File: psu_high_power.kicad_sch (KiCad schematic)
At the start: 4 parts, among them U3 CH224K

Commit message: Final schematic before review.
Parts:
- renumbered C1 to C3, R2 to R3, R1 to R4, U3 to U4
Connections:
- no-connect marks 1 -> 2
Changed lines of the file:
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@@
 	)
 	(no_connect
-		(at 154.94 63.5)
+		(at 92.71 62.23)
+	)
+	(no_connect
+		(at 92.71 59.69)
+	)
+	(wire
+		(pts
+			(xy 99.06 57.15) (xy 99.06 34.29)
+		)
+		(stroke
+			(width 0)
+			(type default)
+		)
+	)
+	(wire
+		(pts
+			(xy 43.18 59.69) (xy 72.39 59.69)
+		)
+		(stroke
+			(width 0)
+			(type default)
+		)
 	)
 	(wire
@@
 	(wire
 		(pts
-			(xy 99.06 57.15) (xy 99.06 34.29)
-		)
-		(stroke
-			(width 0)
-			(type default)
-		)
-	)
-	(wire
-		(pts
-			(xy 43.18 59.69) (xy 72.39 59.69)
-		)
-		(stroke
-			(width 0)
-			(type default)
-		)
-	)
-	(wire
-		(pts
 			(xy 92.71 57.15) (xy 99.06 57.15)
 		)
@@
 	(wire
 		(pts
-			(xy 99.06 34.29) (xy 85.09 34.29)
-		)
-		(stroke
-			(width 0)
-			(type default)
-		)
-	)
-	(wire
-		(pts
 			(xy 92.71 52.07) (xy 116.84 52.07)
 		)
@@
 		(pts
 			(xy 66.04 34.29) (xy 85.09 34.29)
+		)
+		(stroke
+			(width 0)
+			(type default)
+		)
+	)
+	(wire
+		(pts
+			(xy 85.09 34.29) (xy 99.06 34.29)
 		)
 		(stroke
@@
 		(dnp no)
 		(fields_autoplaced yes)
-		(property "Reference" "U3"
+		(property "Reference" "U4"
 			(at 84.6933 67.31 0)
 			(effects
@@
 			(project ""
 				(path "/64404f27-cfd6-41d9-8edb-810ebab8cc14/d3bc8089-8207-4629-875b-88a1d886a985"
-					(reference "U3")
+					(reference "U4")
 					(unit 1)
 				)
@@
 		(on_board yes)
 		(dnp no)
-		(property "Reference" "R2"
+		(property "Reference" "R3"
 			(at 62.23 34.29 90)
 			(effects
@@
 			(project ""
 				(path "/64404f27-cfd6-41d9-8edb-810ebab8cc14/d3bc8089-8207-4629-875b-88a1d886a985"
-					(reference "R2")
+					(reference "R3")
 					(unit 1)
 				)
@@
 		(on_board yes)
 		(dnp no)
-		(property "Reference" "R1"
+		(property "Reference" "R4"
 			(at 62.484 43.434 90)
 			(effects
@@
 			(project ""
 				(path "/64404f27-cfd6-41d9-8edb-810ebab8cc14/d3bc8089-8207-4629-875b-88a1d886a985"
-					(reference "R1")
+					(reference "R4")
 					(unit 1)
 				)
@@
 		(dnp no)
 		(fields_autoplaced yes)
-		(property "Reference" "C1"
+		(property "Reference" "C3"
 			(at 111.76 69.8499 0)
 			(effects
@@
 			(project ""
 				(path "/64404f27-cfd6-41d9-8edb-810ebab8cc14/d3bc8089-8207-4629-875b-88a1d886a985"
-					(reference "C1")
+					(reference "C3")
 					(unit 1)
 				)

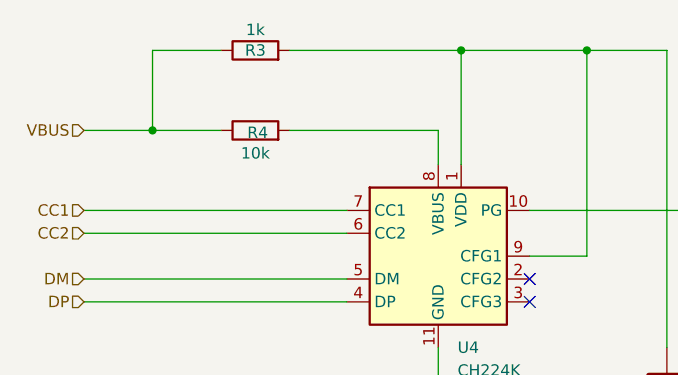
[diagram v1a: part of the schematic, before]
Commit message: Added TVS (SMAJ5.0A) to VBUS-GND Added polyfuses to both PSUs
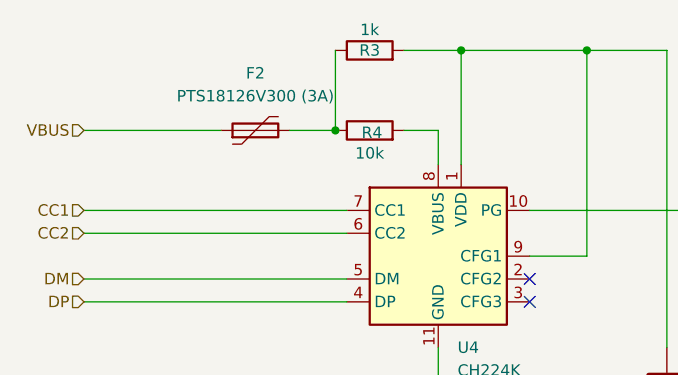
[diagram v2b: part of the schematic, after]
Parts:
- added F2: PTS18126V300 (3A), symbol Device:Polyfuse
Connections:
- net VBUS: now also F2.1; no longer R3.1, R4.1
- new net: F2.2, R3.1, R4.1
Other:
- moved on the sheet: R3, R4
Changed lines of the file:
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@@
 	(paper "A4")
+	(junction
+		(at 71.12 43.18)
+		(diameter 0)
+		(color 0 0 0 0)
+	)
 	(junction
 		(at 82.55 74.93)
@@
 	)
 	(junction
-		(at 50.8 43.18)
+		(at 99.06 34.29)
 		(diameter 0)
 		(color 0 0 0 0)
@@
 		(color 0 0 0 0)
 	)
-	(junction
-		(at 99.06 34.29)
-		(diameter 0)
-		(color 0 0 0 0)
-	)
 	(no_connect
 		(at 92.71 62.23)
@@
 	(wire
 		(pts
+			(xy 78.74 34.29) (xy 85.09 34.29)
+		)
+		(stroke
+			(width 0)
+			(type default)
+		)
+	)
+	(wire
+		(pts
 			(xy 99.06 57.15) (xy 99.06 34.29)
 		)
@@
 	(wire
 		(pts
+			(xy 66.04 43.18) (xy 71.12 43.18)
+		)
+		(stroke
+			(width 0)
+			(type default)
+		)
+	)
+	(wire
+		(pts
 			(xy 92.71 52.07) (xy 116.84 52.07)
 		)
@@
 	(wire
 		(pts
-			(xy 58.42 34.29) (xy 50.8 34.29)
-		)
-		(stroke
-			(width 0)
-			(type default)
-		)
-	)
-	(wire
-		(pts
-			(xy 66.04 43.18) (xy 82.55 43.18)
-		)
-		(stroke
-			(width 0)
-			(type default)
-		)
-	)
-	(wire
-		(pts
 			(xy 82.55 67.31) (xy 82.55 74.93)
 		)
@@
 	(wire
 		(pts
+			(xy 71.12 34.29) (xy 71.12 43.18)
+		)
+		(stroke
+			(width 0)
+			(type default)
+		)
+	)
+	(wire
+		(pts
 			(xy 82.55 80.01) (xy 86.36 80.01)
 		)
@@
 	(wire
 		(pts
-			(xy 50.8 34.29) (xy 50.8 43.18)
+			(xy 78.74 43.18) (xy 82.55 43.18)
 		)
 		(stroke
@@
 	(wire
 		(pts
-			(xy 43.18 43.18) (xy 50.8 43.18)
-		)
-		(stroke
-			(width 0)
-			(type default)
-		)
-	)
-	(wire
-		(pts
-			(xy 66.04 34.29) (xy 85.09 34.29)
+			(xy 43.18 43.18) (xy 58.42 43.18)
 		)
 		(stroke
@@
 		(pts
 			(xy 43.18 52.07) (xy 72.39 52.07)
-		)
-		(stroke
-			(width 0)
-			(type default)
-		)
-	)
-	(wire
-		(pts
-			(xy 50.8 43.18) (xy 58.42 43.18)
 		)
 		(stroke
@@
 			)
 			(justify right)
+		)
+	)
+	(symbol
+		(lib_id "Device:Polyfuse")
+		(at 62.23 43.18 90)
+		(unit 1)
+		(exclude_from_sim no)
+		(in_bom yes)
+		(on_board yes)
+		(dnp no)
+		(fields_autoplaced yes)
+		(property "Reference" "F2"
+			(at 62.23 36.83 90)
+			(effects
+				(font
+					(size 1.27 1.27)
+				)
+			)
+		)
+		(property "Value" "PTS18126V300 (3A)"
+			(at 62.23 39.37 90)
+			(effects
+				(font
+					(size 1.27 1.27)
+				)
+			)
+		)
+		(property "Footprint" ""
+			(at 67.31 41.91 0)
+			(effects
+				(font
+					(size 1.27 1.27)
+				)
+				(justify left)
+				(hide yes)
+			)
+		)
+		(property "Datasheet" "~"
+			(at 62.23 43.18 0)
+			(effects
+				(font
+					(size 1.27 1.27)
+				)
+				(hide yes)
+			)
+		)
+		(property "Description" "Resettable fuse, polymeric positive temperature coefficient"
+			(at 62.23 43.18 0)
+			(effects
+				(font
+					(size 1.27 1.27)
+				)
+				(hide yes)
+			)
+		)
+		(pin "1"
+		)
+		(pin "2"
+		)
+		(instances
+			(project ""
+				(path "/64404f27-cfd6-41d9-8edb-810ebab8cc14/d3bc8089-8207-4629-875b-88a1d886a985"
+					(reference "F2")
+					(unit 1)
+				)
+			)
 		)
 	)
@@
 	(symbol
 		(lib_id "Device:R")
-		(at 62.23 34.29 90)
+		(at 74.93 34.29 90)
 		(unit 1)
 		(exclude_from_sim no)
@@
 		(dnp no)
 		(property "Reference" "R3"
-			(at 62.23 34.29 90)
+			(at 74.93 34.29 90)
 			(effects
 				(font
@@
 		)
 		(property "Value" "1k"
-			(at 62.23 32.004 90)
+			(at 74.93 32.004 90)
 			(effects
 				(font
@@
 		)
 		(property "Footprint" ""
-			(at 62.23 36.068 90)
+			(at 74.93 36.068 90)
 			(effects
 				(font
@@
 		)
 		(property "Datasheet" "~"
-			(at 62.23 34.29 0)
+			(at 74.93 34.29 0)
 			(effects
 				(font
@@
 		)
 		(property "Description" "Resistor"
-			(at 62.23 34.29 0)
+			(at 74.93 34.29 0)
 			(effects
 				(font
@@
 	(symbol
 		(lib_id "Device:R")
-		(at 62.23 43.18 90)
+		(at 74.93 43.18 90)
 		(unit 1)
 		(exclude_from_sim no)
@@
 		(dnp no)
 		(property "Reference" "R4"
-			(at 62.484 43.434 90)
+			(at 75.184 43.434 90)
 			(effects
 				(font
@@
 		)
 		(property "Value" "10k"
-			(at 62.23 45.72 90)
+			(at 74.93 45.72 90)
 			(effects
 				(font
@@
 		)
 		(property "Footprint" ""
-			(at 62.23 44.958 90)
+			(at 74.93 44.958 90)
 			(effects
 				(font
@@
 		)
 		(property "Datasheet" "~"
-			(at 62.23 43.18 0)
+			(at 74.93 43.18 0)
 			(effects
 				(font
@@
 		)
 		(property "Description" "Resistor"
-			(at 62.23 43.18 0)
-			(effects
-				(font
+			(at 74.93 43.18 0)
+			(effects
+				(font

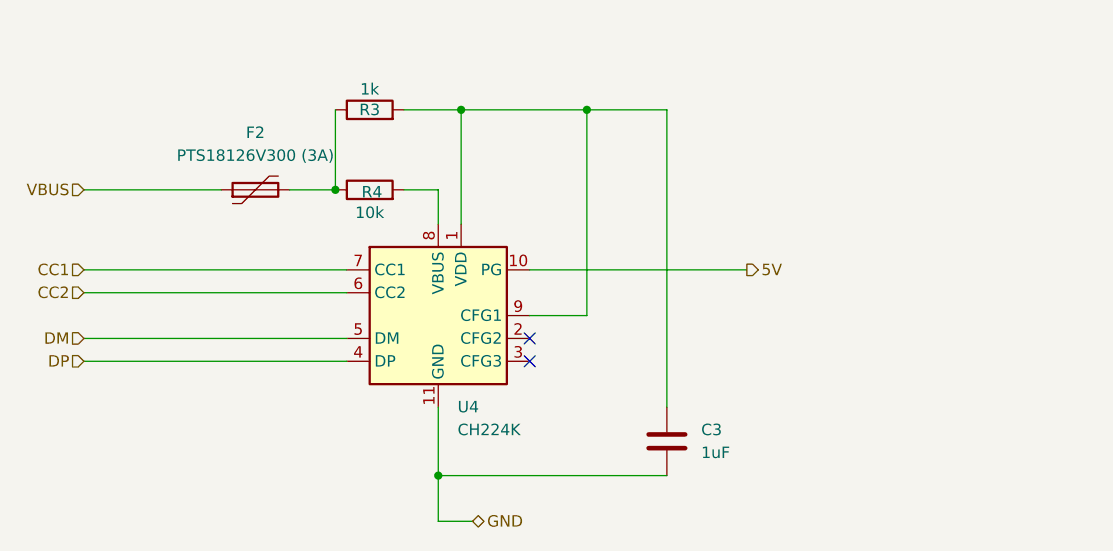
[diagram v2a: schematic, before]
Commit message: Shorted DM-DP on the CK224K (pins don't need to be wired up).
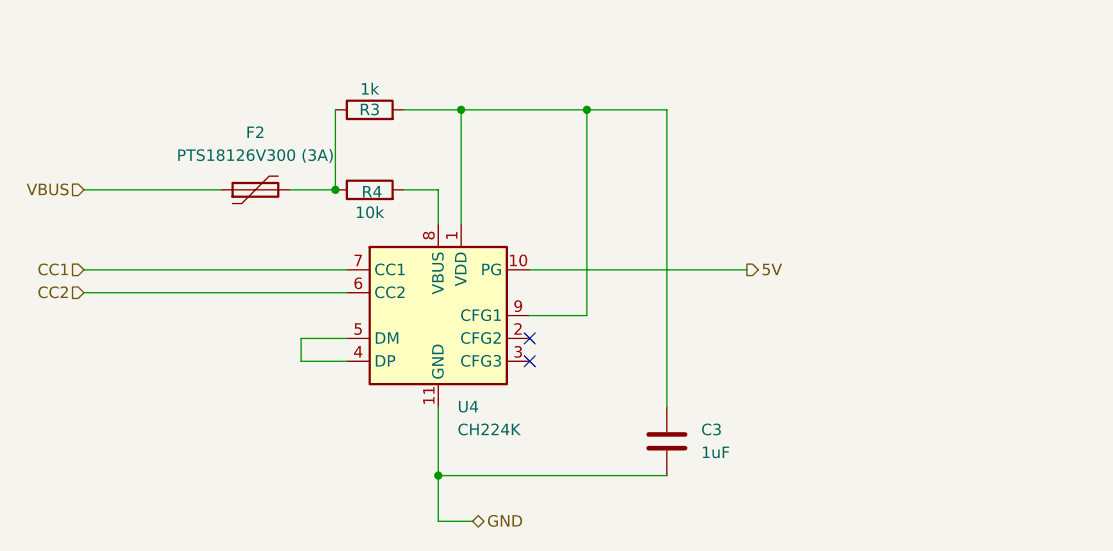
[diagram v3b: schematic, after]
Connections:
- net DP is gone; now on an unnamed net: U4.4 (DP)
- net DM: no longer names the net of U4.5 (DM)
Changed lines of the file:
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@@
-	(wire
-		(pts
-			(xy 43.18 59.69) (xy 72.39 59.69)
-		)
-		(stroke
-			(width 0)
-			(type default)
-		)
-	)
 	(wire
 		(pts
@@
 	(wire
 		(pts
+			(xy 72.39 59.69) (xy 67.31 59.69)
+		)
+		(stroke
+			(width 0)
+			(type default)
+		)
+	)
+	(wire
+		(pts
 			(xy 66.04 43.18) (xy 71.12 43.18)
 		)
@@
 	(wire
 		(pts
+			(xy 67.31 59.69) (xy 67.31 62.23)
+		)
+		(stroke
+			(width 0)
+			(type default)
+		)
+	)
+	(wire
+		(pts
 			(xy 78.74 43.18) (xy 82.55 43.18)
 		)
@@
 	(wire
 		(pts
-			(xy 43.18 62.23) (xy 72.39 62.23)
-		)
-		(stroke
-			(width 0)
-			(type default)
-		)
-	)
-	(wire
-		(pts
 			(xy 107.95 34.29) (xy 99.06 34.29)
+		)
+		(stroke
+			(width 0)
+			(type default)
+		)
+	)
+	(wire
+		(pts
+			(xy 67.31 62.23) (xy 72.39 62.23)
 		)
 		(stroke
@@
 		)
 	)
-	(hierarchical_label "DM"
-		(shape input)
-		(at 43.18 59.69 180)
-		(effects
-			(font
-				(size 1.27 1.27)
-			)
-			(justify right)
-		)
-	)
 	(hierarchical_label "5V"
 		(shape output)
@@
 		)
 	)
-	(hierarchical_label "DP"
-		(shape input)
-		(at 43.18 62.23 180)
-		(effects
-			(font
-				(size 1.27 1.27)
-			)
-			(justify right)
-		)
-	)

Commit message: Fixed design error, 5V is connected to VBUS which is the controlled line.
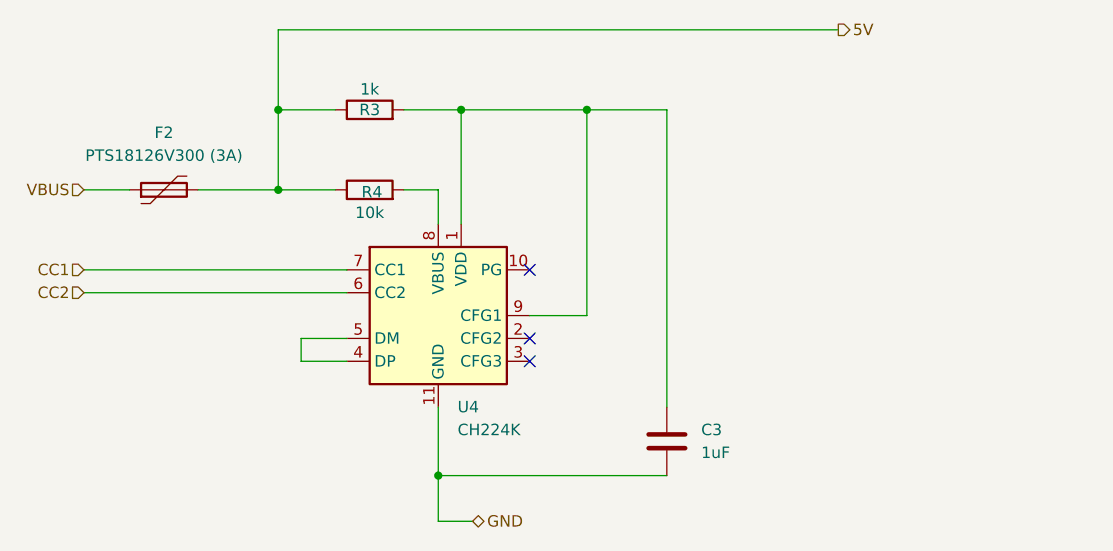
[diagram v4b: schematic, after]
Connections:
- net 5V: now also F2.2, R3.1, R4.1; no longer U4.10 (PG)
- no-connect marks 2 -> 3
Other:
- moved on the sheet: F2
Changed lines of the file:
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@@
 	(paper "A4")
 	(junction
-		(at 71.12 43.18)
+		(at 64.77 34.29)
+		(diameter 0)
+		(color 0 0 0 0)
+	)
+	(junction
+		(at 64.77 43.18)
 		(diameter 0)
 		(color 0 0 0 0)
@@
 		(at 92.71 59.69)
 	)
+	(no_connect
+		(at 92.71 52.07)
+	)
 	(wire
 		(pts
@@
 	(wire
 		(pts
-			(xy 66.04 43.18) (xy 71.12 43.18)
-		)
-		(stroke
-			(width 0)
-			(type default)
-		)
-	)
-	(wire
-		(pts
-			(xy 92.71 52.07) (xy 116.84 52.07)
-		)
-		(stroke
-			(width 0)
-			(type default)
-		)
-	)
-	(wire
-		(pts
 			(xy 82.55 67.31) (xy 82.55 74.93)
 		)
@@
 	(wire
 		(pts
+			(xy 64.77 25.4) (xy 127 25.4)
+		)
+		(stroke
+			(width 0)
+			(type default)
+		)
+	)
+	(wire
+		(pts
 			(xy 82.55 74.93) (xy 107.95 74.93)
 		)
@@
 	(wire
 		(pts
-			(xy 71.12 34.29) (xy 71.12 43.18)
+			(xy 55.88 43.18) (xy 64.77 43.18)
 		)
 		(stroke
@@
 	(wire
 		(pts
+			(xy 64.77 43.18) (xy 71.12 43.18)
+		)
+		(stroke
+			(width 0)
+			(type default)
+		)
+	)
+	(wire
+		(pts
 			(xy 67.31 59.69) (xy 67.31 62.23)
 		)
@@
 	(wire
 		(pts
-			(xy 43.18 43.18) (xy 58.42 43.18)
+			(xy 64.77 34.29) (xy 64.77 43.18)
+		)
+		(stroke
+			(width 0)
+			(type default)
+		)
+	)
+	(wire
+		(pts
+			(xy 64.77 25.4) (xy 64.77 34.29)
 		)
 		(stroke
@@
 		(pts
 			(xy 85.09 34.29) (xy 99.06 34.29)
+		)
+		(stroke
+			(width 0)
+			(type default)
+		)
+	)
+	(wire
+		(pts
+			(xy 43.18 43.18) (xy 48.26 43.18)
+		)
+		(stroke
+			(width 0)
+			(type default)
+		)
+	)
+	(wire
+		(pts
+			(xy 64.77 34.29) (xy 71.12 34.29)
 		)
 		(stroke
@@
 	(hierarchical_label "5V"
 		(shape output)
-		(at 116.84 52.07 0)
+		(at 127 25.4 0)
 		(effects
 			(font
@@
 	(symbol
 		(lib_id "Device:Polyfuse")
-		(at 62.23 43.18 90)
+		(at 52.07 43.18 90)
 		(unit 1)
 		(exclude_from_sim no)
@@
 		(fields_autoplaced yes)
 		(property "Reference" "F2"
-			(at 62.23 36.83 90)
+			(at 52.07 36.83 90)
 			(effects
 				(font
@@
 		)
 		(property "Value" "PTS18126V300 (3A)"
-			(at 62.23 39.37 90)
+			(at 52.07 39.37 90)
 			(effects
 				(font
@@
 		)
 		(property "Footprint" ""
-			(at 67.31 41.91 0)
+			(at 57.15 41.91 0)
 			(effects
 				(font
@@
 		)
 		(property "Datasheet" "~"
-			(at 62.23 43.18 0)
+			(at 52.07 43.18 0)
 			(effects
 				(font
@@
 		)
 		(property "Description" "Resettable fuse, polymeric positive temperature coefficient"
-			(at 62.23 43.18 0)
-			(effects
-				(font
+			(at 52.07 43.18 0)
+			(effects
+				(font

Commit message: Re-labelled all parts.
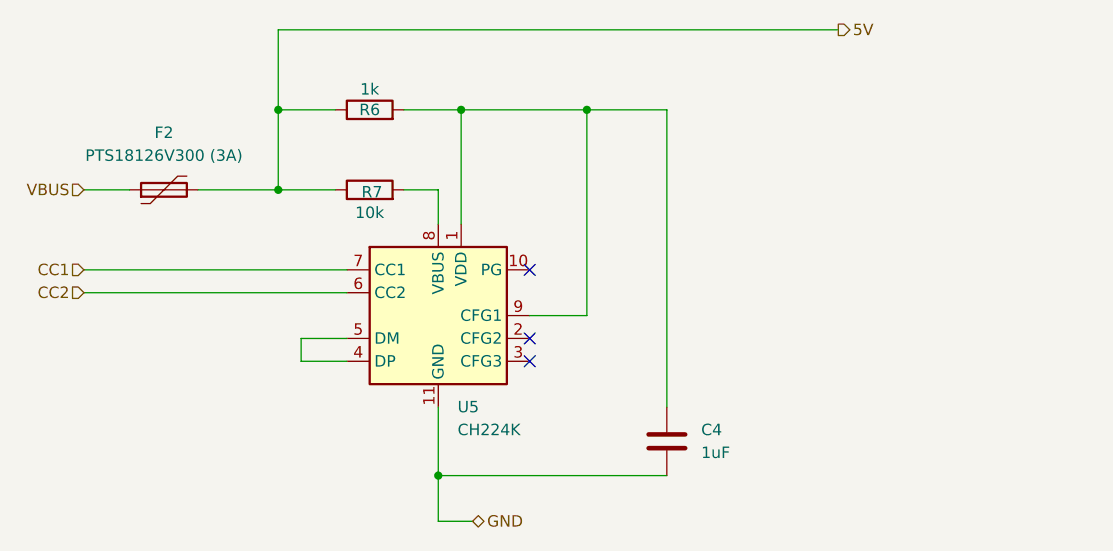
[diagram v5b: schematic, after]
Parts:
- renumbered C3 to C4, R3 to R6, R4 to R7, U4 to U5
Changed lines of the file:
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@@
 		(dnp no)
 		(fields_autoplaced yes)
-		(property "Reference" "U4"
+		(property "Reference" "U5"
 			(at 84.6933 67.31 0)
 			(effects
@@
 			(project ""
 				(path "/64404f27-cfd6-41d9-8edb-810ebab8cc14/d3bc8089-8207-4629-875b-88a1d886a985"
-					(reference "U4")
+					(reference "U5")
 					(unit 1)
 				)
@@
 		(on_board yes)
 		(dnp no)
-		(property "Reference" "R3"
+		(property "Reference" "R6"
 			(at 74.93 34.29 90)
 			(effects
@@
 			(project ""
 				(path "/64404f27-cfd6-41d9-8edb-810ebab8cc14/d3bc8089-8207-4629-875b-88a1d886a985"
-					(reference "R3")
+					(reference "R6")
 					(unit 1)
 				)
@@
 		(on_board yes)
 		(dnp no)
-		(property "Reference" "R4"
+		(property "Reference" "R7"
 			(at 75.184 43.434 90)
 			(effects
@@
 			(project ""
 				(path "/64404f27-cfd6-41d9-8edb-810ebab8cc14/d3bc8089-8207-4629-875b-88a1d886a985"
-					(reference "R4")
+					(reference "R7")
 					(unit 1)
 				)
@@
 		(dnp no)
 		(fields_autoplaced yes)
-		(property "Reference" "C3"
+		(property "Reference" "C4"
 			(at 111.76 69.8499 0)
 			(effects
@@
 			(project ""
 				(path "/64404f27-cfd6-41d9-8edb-810ebab8cc14/d3bc8089-8207-4629-875b-88a1d886a985"
-					(reference "C3")
-					(unit 1)
-				)
+					(reference "C4")
+					(unit 1)
+				)
